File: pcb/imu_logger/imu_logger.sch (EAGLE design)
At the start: 27 parts, among them J1 DM3CS-SF, P1 53398-0310, U1 MAX14591ETAT, U2 LP2985IM5-1.8/NOPB, U3 MAX14591ETAT, U4 MAX14591ETAT, U5 ICM-20948, U6 ICM-20789

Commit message: finished TPMS board and other updates
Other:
- note added: "1.8v regulator"
- note added: "CDH connection"
- note added: "Dual IMU to maximize part availability (one or both may be populated)"
- note added: "Feather M0 Connection (SAMD21)"
- note added: "H3LIS100 high g accel"
- note added: "ICM-20789"
- note added: "ICM-20948"
- note added: "Level shifting"
- note added: "SD card"
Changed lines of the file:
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@@
 <text x="48.26" y="116.84" size="1.778" layer="94">BREAKOUTS</text>
 <text x="60.96" y="86.36" size="1.778" layer="94">100g accel</text>
+<text x="165.1" y="83.82" size="3.81" layer="94">CDH connection</text>
+<text x="180.34" y="165.1" size="3.81" layer="94">SD card</text>
+<text x="27.94" y="170.18" size="3.81" layer="94">Feather M0 Connection (SAMD21)</text>
+<text x="40.64" y="91.44" size="3.81" layer="94">H3LIS100 high g accel </text>
+<wire x1="0" y1="106.68" x2="0" y2="104.14" width="0.3048" layer="94"/>
+<wire x1="0" y1="104.14" x2="147.32" y2="104.14" width="0.3048" layer="94"/>
+<wire x1="147.32" y1="104.14" x2="248.92" y2="104.14" width="0.3048" layer="94"/>
+<wire x1="147.32" y1="104.14" x2="147.32" y2="185.42" width="0.3048" layer="94"/>
+<wire x1="147.32" y1="104.14" x2="147.32" y2="0" width="0.3048" layer="94"/>
 </plain>
 <instances>
@@
 <sheet>
 <plain>
+<text x="22.86" y="175.26" size="3.81" layer="94">Dual IMU to maximize part availability (one or both may be populated)</text>
+<text x="96.52" y="165.1" size="3.81" layer="94">ICM-20948</text>
+<text x="142.24" y="99.06" size="3.81" layer="94">ICM-20789</text>
 </plain>
 <instances>
@@
 <sheet>
 <plain>
+<text x="96.52" y="167.64" size="3.81" layer="94">Level shifting</text>
+<text x="35.56" y="63.5" size="3.81" layer="94">1.8v regulator</text>
+<wire x1="248.92" y1="101.6" x2="0" y2="101.6" width="0.508" layer="94"/>
 </plain>
 <instances>

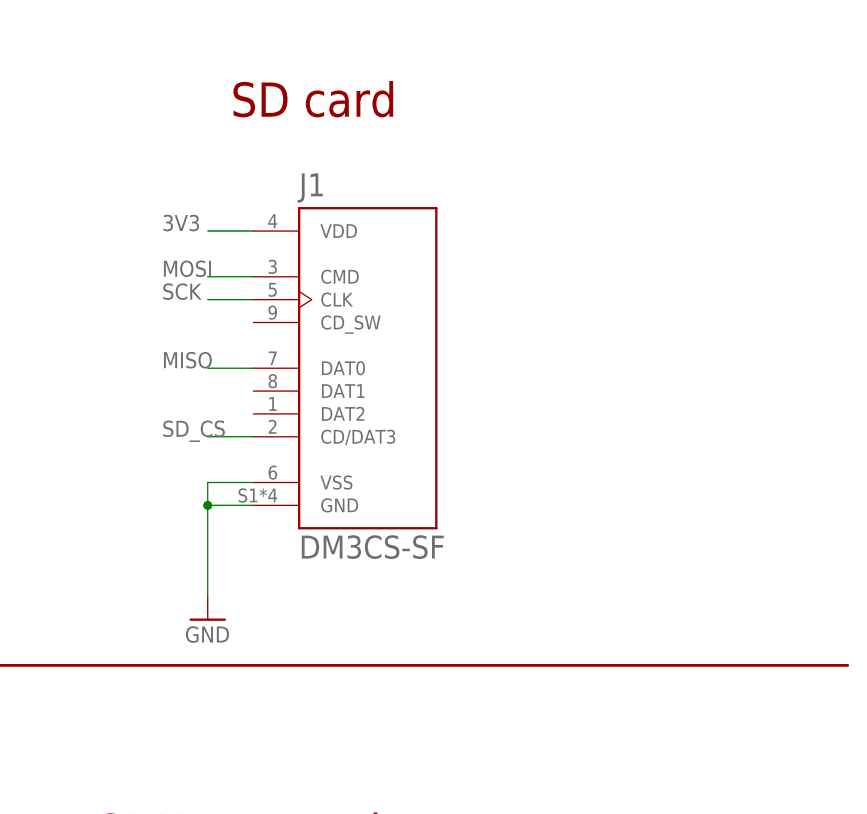
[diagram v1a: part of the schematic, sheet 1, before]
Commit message: add imu board cam files and replace sd card holder
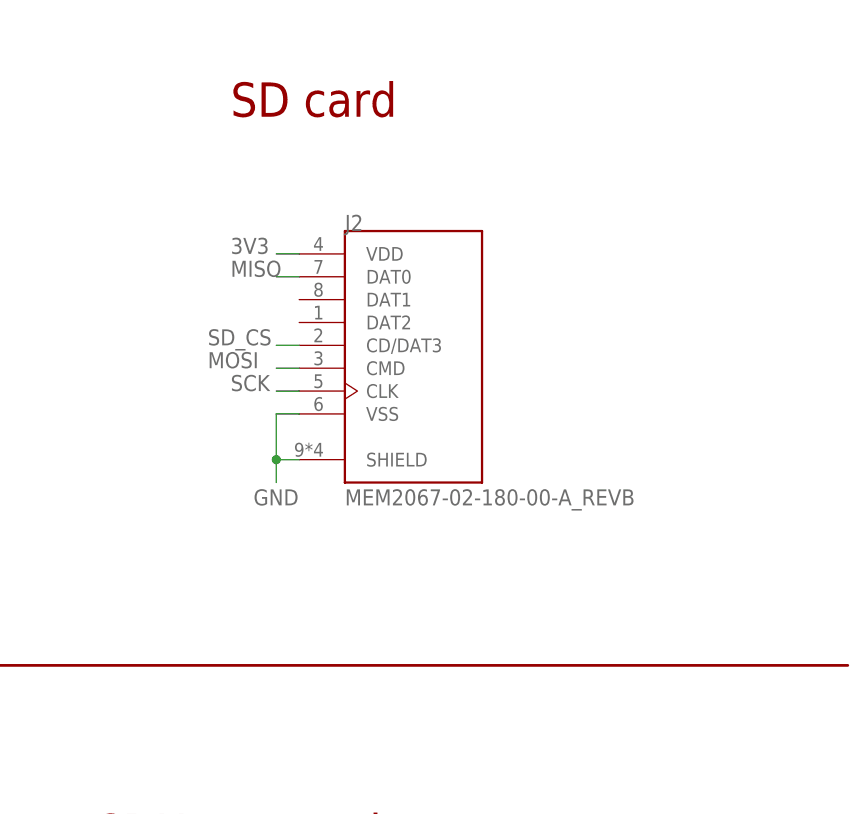
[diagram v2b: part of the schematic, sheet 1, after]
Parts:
- removed J1: DM3CS-SF, DM3CS-SF:DM3CS-SF
- added J2: MEM2067-02-180-00-A_REVB, MEM20267:MEM2067-02-180-00-A_REVB
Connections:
- net 3V3: now also J2.VDD; no longer J1.VDD
- net GND: now also J2.SHIELD, J2.VSS; no longer J1.GND, J1.VSS
- net MISO: now also J2.DAT0; no longer J1.DAT0
- net MOSI: now also J2.CMD; no longer J1.CMD
- net SCK: now also J2.CLK; no longer J1.CLK
- net SD_CS: now also J2.CD/DAT3; no longer J1.CD/DAT3
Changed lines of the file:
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@@
 <layer number="115" name="ReferenceISLANDS" color="7" fill="1" visible="yes" active="yes"/>
 <layer number="116" name="Patch_BOT" color="9" fill="4" visible="yes" active="yes"/>
+<layer number="117" name="BACKMAAT1" color="7" fill="1" visible="yes" active="yes"/>
 <layer number="118" name="Rect_Pads" color="7" fill="1" visible="no" active="no"/>
+<layer number="119" name="KAP_TEKEN" color="7" fill="1" visible="yes" active="yes"/>
+<layer number="120" name="KAP_MAAT1" color="7" fill="1" visible="yes" active="yes"/>
 <layer number="121" name="sName" color="7" fill="1" visible="yes" active="yes"/>
 <layer number="122" name="_bPlace" color="7" fill="1" visible="yes" active="yes"/>
@@
 <layer number="128" name="_bValues" color="7" fill="1" visible="yes" active="yes"/>
 <layer number="129" name="Mask" color="7" fill="1" visible="yes" active="yes"/>
+<layer number="130" name="SMDSTROOK" color="7" fill="1" visible="yes" active="yes"/>
 <layer number="131" name="tAdjust" color="7" fill="1" visible="no" active="yes"/>
 <layer number="132" name="bAdjust" color="7" fill="1" visible="no" active="yes"/>
+<layer number="133" name="bottom_silk" color="7" fill="1" visible="yes" active="yes"/>
 <layer number="144" name="Drill_legend" color="7" fill="1" visible="yes" active="yes"/>
 <layer number="150" name="Notes" color="7" fill="1" visible="yes" active="yes"/>
@@
 <class number="0" name="default" width="0" drill="0">
 </class>
+<class number="2" name="gnd" width="0.254" drill="0">
+</class>
 </classes>
 <parts>
@@
 <part name="JP3" library="microbuilder" deviceset="HEADER-1X12" device=""/>
 <part name="GND11" library="supply1" deviceset="GND" device=""/>
-<part name="J1" library="DM3CS-SF" deviceset="DM3CS-SF" device=""/>
 <part name="C18" library="rcl" library_urn="urn:adsk.eagle:library:334" deviceset="C-US" device="C0603" package3d_urn="urn:adsk.eagle:package:23616/2" value="0.1uF"/>
 <part name="C19" library="rcl" library_urn="urn:adsk.eagle:library:334" deviceset="C-US" device="C0603" package3d_urn="urn:adsk.eagle:package:23616/2" value="2.2uF"/>
@@
 <part name="U3" library="MAX14591ETAT" deviceset="MAX14591ETAT" device=""/>
 <part name="U4" library="MAX14591ETAT" deviceset="MAX14591ETAT" device=""/>
-<part name="GND1" library="supply1" deviceset="GND" device=""/>
 <part name="U6" library="ICM-20789" deviceset="ICM-20789" device=""/>
 <part name="C5" library="rcl" library_urn="urn:adsk.eagle:library:334" deviceset="C-EU" device="C0603" package3d_urn="urn:adsk.eagle:package:23616/2" value="0.1uF"/>
@@
 <part name="C8" library="rcl" library_urn="urn:adsk.eagle:library:334" deviceset="C-EU" device="C0603" package3d_urn="urn:adsk.eagle:package:23616/2" value="2.2uF"/>
 <part name="P1" library="con-molex-picoblade" library_urn="urn:adsk.eagle:library:28185481" deviceset="53398-0310" device="" package3d_urn="urn:adsk.eagle:package:28185543/1"/>
+<part name="J2" library="MEM20267" deviceset="MEM2067-02-180-00-A_REVB" device=""/>
 </parts>
 <sheets>
@@
 <attribute name="DRAWING_NAME" x="165.1" y="19.05" size="2.54" layer="94"/>
 </instance>
-<instance part="J1" gate="G$1" x="195.58" y="137.16" smashed="yes">
-<attribute name="NAME" x="187.95178125" y="156.2576" size="2.54725" layer="95"/>
-<attribute name="VALUE" x="187.944340625" y="116.0092" size="2.548809375" layer="96"/>
-</instance>
 <instance part="U$19" gate="G$1" x="38.1" y="149.86" smashed="yes" rot="R90">
 <attribute name="VALUE" x="37.084" y="148.336" size="1.27" layer="96" rot="R90"/>
@@
 <attribute name="VALUE" x="86.36" y="111.76" size="1.778" layer="96"/>
 </instance>
-<instance part="GND1" gate="1" x="177.8" y="109.22" smashed="yes">
-<attribute name="VALUE" x="175.26" y="106.68" size="1.778" layer="96"/>
-</instance>
 <instance part="P1" gate="G$1" x="182.88" y="73.66" smashed="yes">
 <attribute name="NAME" x="181.61" y="79.375" size="1.778" layer="95"/>
 <attribute name="VALUE" x="181.61" y="66.04" size="1.778" layer="95"/>
+</instance>
+<instance part="J2" gate="G$1" x="193.04" y="139.7" smashed="yes">
+<attribute name="NAME" x="193.04" y="152.4117" size="1.779640625" layer="95"/>
+<attribute name="VALUE" x="193.04" y="121.9174" size="1.778259375" layer="96"/>
 </instance>
 </instances>
@@
 </segment>
 <segment>
-<pinref part="J1" gate="G$1" pin="GND"/>
-<wire x1="182.88" y1="121.92" x2="177.8" y2="121.92" width="0.1524" layer="91"/>
-<wire x1="177.8" y1="121.92" x2="177.8" y2="111.76" width="0.1524" layer="91"/>
-<pinref part="GND1" gate="1" pin="GND"/>
-<pinref part="J1" gate="G$1" pin="VSS"/>
-<wire x1="182.88" y1="124.46" x2="177.8" y2="124.46" width="0.1524" layer="91"/>
-<wire x1="177.8" y1="124.46" x2="177.8" y2="121.92" width="0.1524" layer="91"/>
-<junction x="177.8" y="121.92"/>
-</segment>
-<segment>
 <pinref part="P1" gate="G$1" pin="3"/>
 <wire x1="177.8" y1="71.12" x2="172.72" y2="71.12" width="0.1524" layer="91"/>
 <label x="170.18" y="71.12" size="1.778" layer="95"/>
+</segment>
+<segment>
+<pinref part="J2" gate="G$1" pin="VSS"/>
+<wire x1="187.96" y1="132.08" x2="185.42" y2="132.08" width="0.1524" layer="91"/>
+<pinref part="J2" gate="G$1" pin="SHIELD"/>
+<wire x1="185.42" y1="132.08" x2="185.42" y2="127" width="0.1524" layer="91"/>
+<wire x1="185.42" y1="127" x2="187.96" y2="127" width="0.1524" layer="91"/>
+<wire x1="185.42" y1="127" x2="185.42" y2="124.46" width="0.1524" layer="91"/>
+<junction x="185.42" y="127"/>
+<label x="182.88" y="121.92" size="1.778" layer="95"/>
 </segment>
 </net>
@@
 </segment>
 <segment>
-<pinref part="J1" gate="G$1" pin="VDD"/>
-<wire x1="182.88" y1="152.4" x2="177.8" y2="152.4" width="0.1524" layer="91"/>
-<label x="172.72" y="152.4" size="1.778" layer="95"/>
-</segment>
-<segment>
 <pinref part="+3V1" gate="G$1" pin="+3V3"/>
 <wire x1="88.9" y1="154.94" x2="88.9" y2="152.4" width="0.1524" layer="91"/>
@@
 <label x="88.9" y="152.4" size="1.778" layer="95"/>
 </segment>
+<segment>
+<pinref part="J2" gate="G$1" pin="VDD"/>
+<wire x1="187.96" y1="149.86" x2="185.42" y2="149.86" width="0.1524" layer="91"/>
+<label x="180.34" y="149.86" size="1.778" layer="95"/>
+</segment>
 </net>
 <net name="MOSI" class="0">
@@
 </segment>
 <segment>
-<pinref part="J1" gate="G$1" pin="CMD"/>
-<wire x1="182.88" y1="147.32" x2="177.8" y2="147.32" width="0.1524" layer="91"/>
-<label x="172.72" y="147.32" size="1.778" layer="95"/>
+<pinref part="J2" gate="G$1" pin="CMD"/>
+<wire x1="187.96" y1="137.16" x2="185.42" y2="137.16" width="0.1524" layer="91"/>
+<label x="177.8" y="137.16" size="1.778" layer="95"/>
 </segment>
 </net>
@@
 </segment>
 <segment>
-<pinref part="J1" gate="G$1" pin="DAT0"/>
-<wire x1="182.88" y1="137.16" x2="177.8" y2="137.16" width="0.1524" layer="91"/>
-<label x="172.72" y="137.16" size="1.778" layer="95"/>
+<pinref part="J2" gate="G$1" pin="DAT0"/>
+<wire x1="187.96" y1="147.32" x2="185.42" y2="147.32" width="0.1524" layer="91"/>
+<label x="180.34" y="147.32" size="1.778" layer="95"/>
 </segment>
 </net>
@@
 </segment>
 <segment>
-<pinref part="J1" gate="G$1" pin="CLK"/>
-<wire x1="182.88" y1="144.78" x2="177.8" y2="144.78" width="0.1524" layer="91"/>
-<label x="172.72" y="144.78" size="1.778" layer="95"/>
+<pinref part="J2" gate="G$1" pin="CLK"/>
+<wire x1="187.96" y1="134.62" x2="185.42" y2="134.62" width="0.1524" layer="91"/>
+<label x="180.34" y="134.62" size="1.778" layer="95"/>
 </segment>
 </net>
@@
 <net name="SD_CS" class="0">
 <segment>
-<pinref part="J1" gate="G$1" pin="CD/DAT3"/>
-<wire x1="182.88" y1="129.54" x2="177.8" y2="129.54" width="0.1524" layer="91"/>
-<label x="172.72" y="129.54" size="1.778" layer="95"/>
-</segment>
-<segment>
 <wire x1="48.26" y1="139.7" x2="68.58" y2="139.7" width="0.1524" layer="91"/>
 <label x="48.26" y="139.7" size="1.778" layer="95"/>
 <pinref part="JP3" gate="G$1" pin="7"/>
 </segment>
-</net>
+<segment>
+<pinref part="J2" gate="G$1" pin="CD/DAT3"/>
+<wire x1="187.96" y1="139.7" x2="185.42" y2="139.7" width="0.1524" layer="91"/>
+<label x="177.8" y="139.7" size="1.778" layer="95"/>
+</segment>
+</net>
